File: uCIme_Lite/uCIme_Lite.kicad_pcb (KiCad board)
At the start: 4 copper layers, 65 x 56 mm, 71 parts, among them J1 POWER_MODES, J11 SERIAL_MODE, J12 SERIAL_VOLTAGE_SELECT, J2 JACK_POWER_IN, J3 USB_POWER_IN, J4 USB_PC, J6 5V_ENABLE, J7 SERIAL_AND_GPIO, J8 JACK_POWER_OUT, J9 USB_POWER_OUT, Q1 BSS138, Q2 BUK7M27-80EX, Q3 BUK7M27-80EX, Q4 BSS138, Q5 BSS138, Q6 BSS138, Q7 BSS138, Q8 BSS138, U1 LM74502, U2 LM74502, U3 AP2204K-ADJ, U4 AP2204K-ADJ, U5 FT230XS, U6 TXB0104D

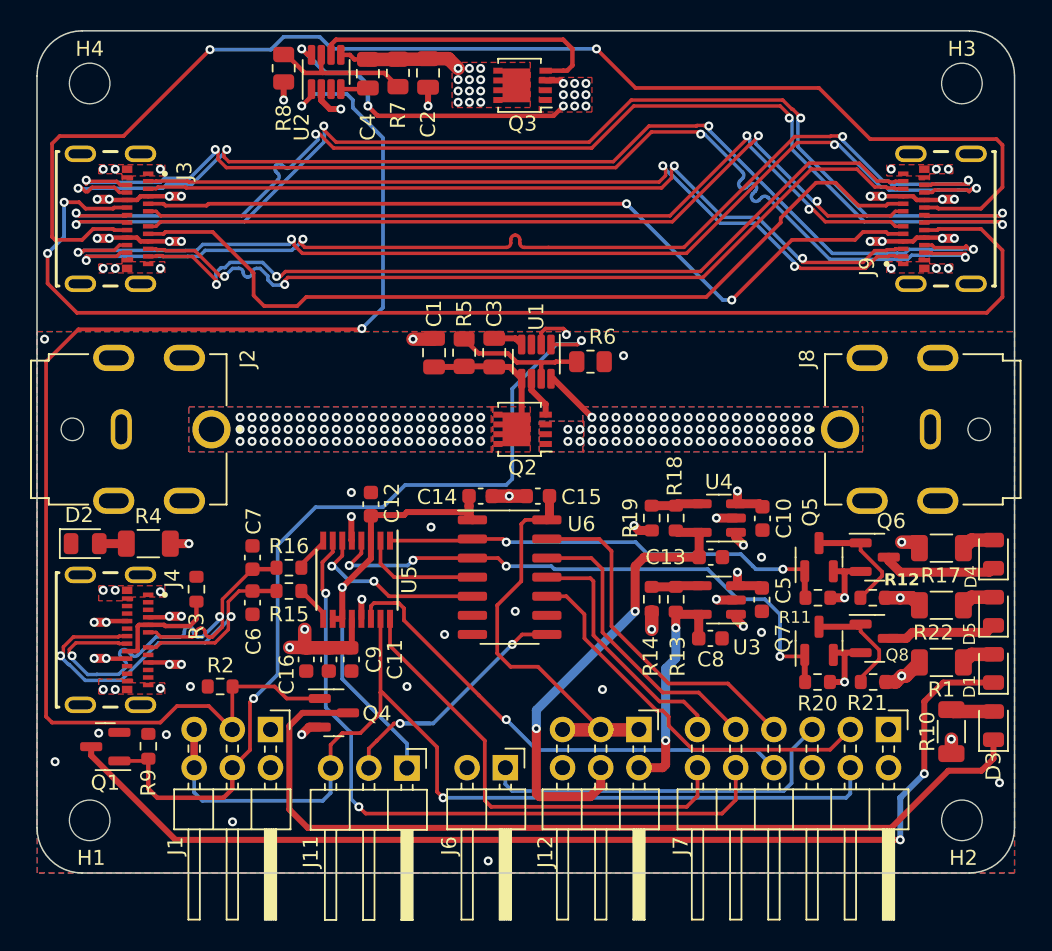
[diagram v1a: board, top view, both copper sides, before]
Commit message: lite: Added board usage documentation on PCB silkscreen.
Signed-off-by: Adrien Ricciardi <aricciardi@baylibre.com>
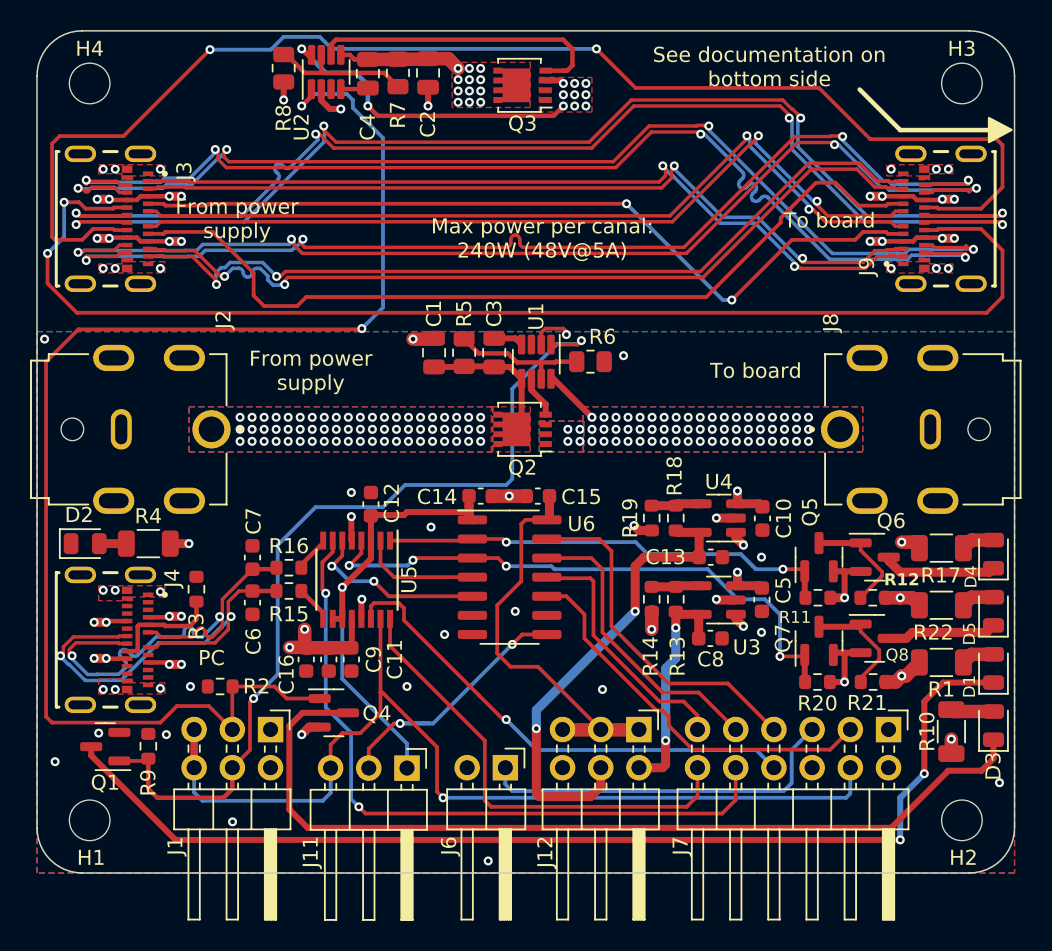
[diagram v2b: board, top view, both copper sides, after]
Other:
- board text added: "+5V"
- board text added: "+5V (see J6)"
- board text added: "/CTS"
- board text added: "/RTS"
- board text added: "1"
- board text added: "2"
- board text added: "3"
- board text added: "4"
- board text added: "5"
- board text added: "6"
- board text added: "Fit 1-2: UART always enabled Fit 2-3: UART enabled with channel"
- board text added: "Fit 1-2: UART voltage = +1.8V Fit 3-4: UART voltage = +3.3V Fit 5-6: UART voltage = +5V"
- board text added: "Fit 1-3: always enable USB channel power Fit 3-5: control USB channel power with GPIO Unfit 1-3-5: disable USB channel power Fit 2-4: always enable jack channel power Fit 4-6: control jack channel power with GPIO Unfit 2-4-6: disable jack channel power"
- board text added: "Fit to enable +5V on UART header"
- board text added: "From power supply"
- board text added: "GND"
- board text added: "GPIO0"
- board text added: "GPIO1"
- board text added: "GPIO2"
- board text added: "GPIO3"
- board text added: "JACK"
- board text added: "Max power per canal: 240W (48V@5A)"
- board text added: "PC"
- board text added: "PC USB"
- board text added: "RX"
- board text added: "See documentation on bottom side"
- board text added: "TX"
- board text added: "To board"
- board text added: "USB"
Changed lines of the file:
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@@
     (property "ki_keywords" "R res resistor")
     (attr smd)
-    (fp_text reference "R2" (at -0.025 1.4) (layer "F.SilkS")
+    (fp_text reference "R2" (at -2.425 0) (layer "F.SilkS")
         (effects (font (size 1 1) (thickness 0.15)))
     )
@@
     (property "Sheetname" "")
     (attr through_hole)
-    (fp_text reference "J2" (at -4.7 -2.4 90) (layer "F.SilkS")
+    (fp_text reference "J2" (at -7.3 -0.8 90) (layer "F.SilkS")
         (effects (font (size 1 1) (thickness 0.15)))
     )
@@
     (property "Sheetname" "")
     (attr through_hole)
-    (fp_text reference "J8" (at 4.7 -2.2 90) (layer "F.SilkS")
+    (fp_text reference "J8" (at 7.1 -0.6 90) (layer "F.SilkS")
         (effects (font (size 1 1) (thickness 0.15)))
     )
@@
     )
   )
+  (gr_rect (start 83.6 105) (end 90.65 107)
+    (stroke (width 0.15) (type solid)) (fill solid) (layer "B.SilkS"))
+  (gr_rect (start 74.475 102.4) (end 81.575 107)
+    (stroke (width 0.15) (type solid)) (fill solid) (layer "B.SilkS"))
+  (gr_line (start 87.3 105.1) (end 87.3 104.1)
+    (stroke (width 0.4) (type default)) (layer "B.SilkS"))
+  (gr_line (start 79.7 102.6) (end 79.7 72.2)
+    (stroke (width 0.4) (type default)) (layer "B.SilkS"))
+  (gr_rect (start 98.95 102.4) (end 106.1 107)
+    (stroke (width 0.15) (type solid)) (fill solid) (layer "B.SilkS"))
+  (gr_line (start 94.7 105.2) (end 94.7 104.2)
+    (stroke (width 0.4) (type default)) (layer "B.SilkS"))
+  (gr_rect (start 92.6 105) (end 97.2 107)
+    (stroke (width 0.15) (type solid)) (fill solid) (layer "B.SilkS"))
+  (gr_line (start 104 102.6) (end 104 100.2)
+    (stroke (width 0.4) (type default)) (layer "B.SilkS"))
+  (gr_line (start 122.4 63.6) (end 128.4 63.6)
+    (stroke (width 0.3) (type default)) (layer "F.SilkS"))
+  (gr_line (start 119.7 60.9) (end 122.4 63.6)
+    (stroke (width 0.3) (type default)) (layer "F.SilkS"))
+  (gr_poly
+    (pts
+      (xy 129.798043 63.587574)
+      (xy 128.3 62.8)
+      (xy 128.3 64.4)
+    )
+    (stroke (width 0.15) (type solid)) (fill solid) (layer "F.SilkS"))
   (gr_arc (start 130 110) (mid 129.12132 112.12132) (end 127 113)
     (stroke (width 0.1) (type default)) (layer "Edge.Cuts"))
@@
   (gr_arc (start 65 60) (mid 65.87868 57.87868) (end 68 57)
     (stroke (width 0.1) (type default)) (layer "Edge.Cuts"))
+  (gr_text "Fit to enable +5V on UART header" (at 94 104 270) (layer "B.SilkS" knockout)
+    (effects (font (size 1 1) (thickness 0.15)) (justify left bottom mirror))
+  )
+  (gr_text "6" (at 100.4 108.4) (layer "B.SilkS")
+    (effects (font (size 1 1) (thickness 0.15)) (justify left bottom mirror))
+  )
+  (gr_text "GPIO1" (at 113.4 107.4 270) (layer "B.SilkS" knockout)
+    (effects (font (size 1 1) (thickness 0.15)) (justify right bottom mirror))
+  )
+  (gr_text "+5V" (at 115.9 107.4 270) (layer "B.SilkS" knockout)
+    (effects (font (size 1 1) (thickness 0.15)) (justify right bottom mirror))
+  )
+  (gr_text "GND" (at 120.9 102 270) (layer "B.SilkS" knockout)
+    (effects (font (size 1 1) (thickness 0.15)) (justify left bottom mirror))
+  )
+  (gr_text "RX" (at 129.4 92.4) (layer "B.SilkS" knockout)
+    (effects (font (size 1 1) (thickness 0.15)) (justify left bottom mirror))
+  )
+  (gr_text "3" (at 85 108.4) (layer "B.SilkS")
+    (effects (font (size 1 1) (thickness 0.15)) (justify left bottom mirror))
+  )
+  (gr_text "GPIO0" (at 118.4 107.4 270) (layer "B.SilkS" knockout)
+    (effects (font (size 1 1) (thickness 0.15)) (justify right bottom mirror))
+  )
+  (gr_text "GPIO3" (at 108.2 107.4 270) (layer "B.SilkS" knockout)
+    (effects (font (size 1 1) (thickness 0.15)) (justify right bottom mirror))
+  )
+  (gr_text "5" (at 75.8 102.2) (layer "B.SilkS")
+    (effects (font (size 1 1) (thickness 0.15)) (justify left bottom mirror))
+  )
+  (gr_text "GND" (at 120.9 107.4 270) (layer "B.SilkS" knockout)
+    (effects (font (size 1 1) (thickness 0.15)) (justify right bottom mirror))
+  )
+  (gr_text "PC USB" (at 71.6 91.8) (layer "B.SilkS" knockout)
+    (effects (font (size 1 1) (thickness 0.15)) (justify left bottom mirror))
+  )
+  (gr_text "1" (at 81 102.2) (layer "B.SilkS")
+    (effects (font (size 1 1) (thickness 0.15)) (justify left bottom mirror))
+  )
+  (gr_text "5" (at 100.4 102.2) (layer "B.SilkS")
+    (effects (font (size 1 1) (thickness 0.15)) (justify left bottom mirror))
+  )
+  (gr_text "3" (at 103 102.2) (layer "B.SilkS")
+    (effects (font (size 1 1) (thickness 0.15)) (justify left bottom mirror))
+  )
+  (gr_text "4" (at 78.4 108.4) (layer "B.SilkS")
+    (effects (font (size 1 1) (thickness 0.15)) (justify left bottom mirror))
+  )
+  (gr_text "TX" (at 129.4 96.2) (layer "B.SilkS" knockout)
+    (effects (font (size 1 1) (thickness 0.15)) (justify left bottom mirror))
+  )
+  (gr_text "TX" (at 113.4 102 270) (layer "B.SilkS" knockout)
+    (effects (font (size 1 1) (thickness 0.15)) (justify left bottom mirror))
+  )
+  (gr_text "6" (at 75.8 108.4) (layer "B.SilkS")
+    (effects (font (size 1 1) (thickness 0.15)) (justify left bottom mirror))
+  )
+  (gr_text "2" (at 87.6 108.4) (layer "B.SilkS")
+    (effects (font (size 1 1) (thickness 0.15)) (justify left bottom mirror))
+  )
+  (gr_text "Fit 1-3: always enable USB channel power\nFit 3-5: control USB channel power with GPIO\nUnfit 1-3-5: disable USB channel power\nFit 2-4: always enable jack channel power\nFit 4-6: control jack channel power with GPIO\nUnfit 2-4-6: disable jack channel power" (at 111.4 72.2) (layer "B.SilkS" knockout)
+    (effects (font (size 1 1) (thickness 0.15)) (justify left bottom mirror))
+  )
+  (gr_text "1" (at 90 108.4) (layer "B.SilkS")
+    (effects (font (size 1 1) (thickness 0.15)) (justify left bottom mirror))
+  )
+  (gr_text "3" (at 78.4 102.2) (layer "B.SilkS")
+    (effects (font (size 1 1) (thickness 0.15)) (justify left bottom mirror))
+  )
+  (gr_text "Fit 1-2: UART always enabled\nFit 2-3: UART enabled with channel" (at 85.8 104 270) (layer "B.SilkS" knockout)
+    (effects (font (size 1 1) (thickness 0.15)) (justify left bottom mirror))
+  )
+  (gr_text "4" (at 103 108.4) (layer "B.SilkS")
+    (effects (font (size 1 1) (thickness 0.15)) (justify left bottom mirror))
+  )
+  (gr_text "+5V (see J6)" (at 115.9 102 270) (layer "B.SilkS" knockout)
+    (effects (font (size 1 1) (thickness 0.15)) (justify left bottom mirror))
+  )
+  (gr_text "GPIO2" (at 110.8 107.4 270) (layer "B.SilkS" knockout)
+    (effects (font (size 1 1) (thickness 0.15)) (justify right bottom mirror))
+  )
+  (gr_text "Fit 1-2: UART voltage = +1.8V\nFit 3-4: UART voltage = +3.3V \nFit 5-6: UART voltage = +5V " (at 100.2 100 270) (layer "B.SilkS" knockout)
+    (effects (font (size 1 1) (thickness 0.15)) (justify left bottom mirror))
+  )
+  (gr_text "1" (at 96.6 108.4) (layer "B.SilkS")
+    (effects (font (size 1 1) (thickness 0.15)) (justify left bottom mirror))
+  )
+  (gr_text "/RTS" (at 108.2 102 270) (layer "B.SilkS" knockout)
+    (effects (font (size 1 1) (thickness 0.15)) (justify left bottom mirror))
+  )
+  (gr_text "2" (at 105.6 108.4) (layer "B.SilkS")
+    (effects (font (size 1 1) (thickness 0.15)) (justify left bottom mirror))
+  )
+  (gr_text "2" (at 81 108.4) (layer "B.SilkS")
+    (effects (font (size 1 1) (thickness 0.15)) (justify left bottom mirror))
+  )
+  (gr_text "1" (at 105.6 102.2) (layer "B.SilkS")
+    (effects (font (size 1 1) (thickness 0.15)) (justify left bottom mirror))
+  )
+  (gr_text "2" (at 94 108.4) (layer "B.SilkS")
+    (effects (font (size 1 1) (thickness 0.15)) (justify left bottom mirror))
+  )
+  (gr_text "JACK" (at 129.4 100) (layer "B.SilkS" knockout)
+    (effects (font (size 1 1) (thickness 0.15)) (justify left bottom mirror))
+  )
+  (gr_text "USB" (at 129.4 103.8) (layer "B.SilkS" knockout)
+    (effects (font (size 1 1) (thickness 0.15)) (justify left bottom mirror))
+  )
+  (gr_text "/CTS" (at 118.4 102 270) (layer "B.SilkS" knockout)
+    (effects (font (size 1 1) (thickness 0.15)) (justify left bottom mirror))
+  )
+  (gr_text "RX" (at 110.8 102 270) (layer "B.SilkS" knockout)
+    (effects (font (size 1 1) (thickness 0.15)) (justify left bottom mirror))
+  )
+  (gr_text "See documentation on\nbottom side" (at 113.7 60.8) (layer "F.SilkS" knockout)
+    (effects (font (size 1 1) (thickness 0.15)) (justify bottom))
+  )
+  (gr_text "To board" (at 112.8 80.2) (layer "F.SilkS" knockout)
+    (effects (font (size 1 1) (thickness 0.15)) (justify bottom))
+  )
+  (gr_text "To board" (at 117.7 70.2) (layer "F.SilkS" knockout)
+    (effects (font (size 1 1) (thickness 0.15)) (justify bottom))
+  )
+  (gr_text "Max power per canal:\n240W (48V@5A)" (at 98.6 72.2) (layer "F.SilkS" knockout)
+    (effects (font (size 1 1) (thickness 0.15)) (justify bottom))
+  )
+  (gr_text "From power\nsupply" (at 83.2 81) (layer "F.SilkS" knockout)
+    (effects (font (size 1 1) (thickness 0.15)) (justify bottom))
+  )
+  (gr_text "PC" (at 76.6 99.3) (layer "F.SilkS" knockout)
+    (effects (font (size 1 1) (thickness 0.15)) (justify bottom))
+  )
+  (gr_text "From power\nsupply" (at 78.3 70.9) (layer "F.SilkS" knockout)
+    (effects (font (size 1 1) (thickness 0.15)) (justify bottom))
+  )
   (segment (start 97.225 83.155) (end 96.88 83.5) (width 0.4) (layer "F.Cu") (net 1))
   (segment (start 95.4 79.35) (end 96.4375 79.35) (width 0.4) (layer "F.Cu") (net 1))

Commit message: lite: Changed the serial RX and TX led names in schematic and PCB to match the previous change made to ease routing.
Signed-off-by: Adrien Ricciardi <aricciardi@baylibre.com>
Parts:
- D4: value UART_RX -> UART_TX
- D5: value UART_TX -> UART_RX
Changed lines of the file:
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@@
         (effects (font (size 0.8 0.8) (thickness 0.15)))
     )
-    (fp_text value "UART_TX" (at 0 1.65 90) (layer "F.Fab") hide
+    (fp_text value "UART_RX" (at 0 1.65 90) (layer "F.Fab") hide
         (effects (font (size 1 1) (thickness 0.15)))
     )
@@
         (effects (font (size 0.8 0.8) (thickness 0.15)))
     )
-    (fp_text value "UART_RX" (at 0 1.65 90) (layer "F.Fab") hide
-        (effects (font (size 1 1) (thickness 0.15)))
-    )
+    (fp_text value "UART_TX" (at 0 1.65 90) (layer "F.Fab") hide
+        (effects (font (size 1 1) (thickness 0.15)))
+    )
